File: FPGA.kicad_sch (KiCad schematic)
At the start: 19 parts, among them U3 XC7A100T-FTG256, U5 S25FL127S

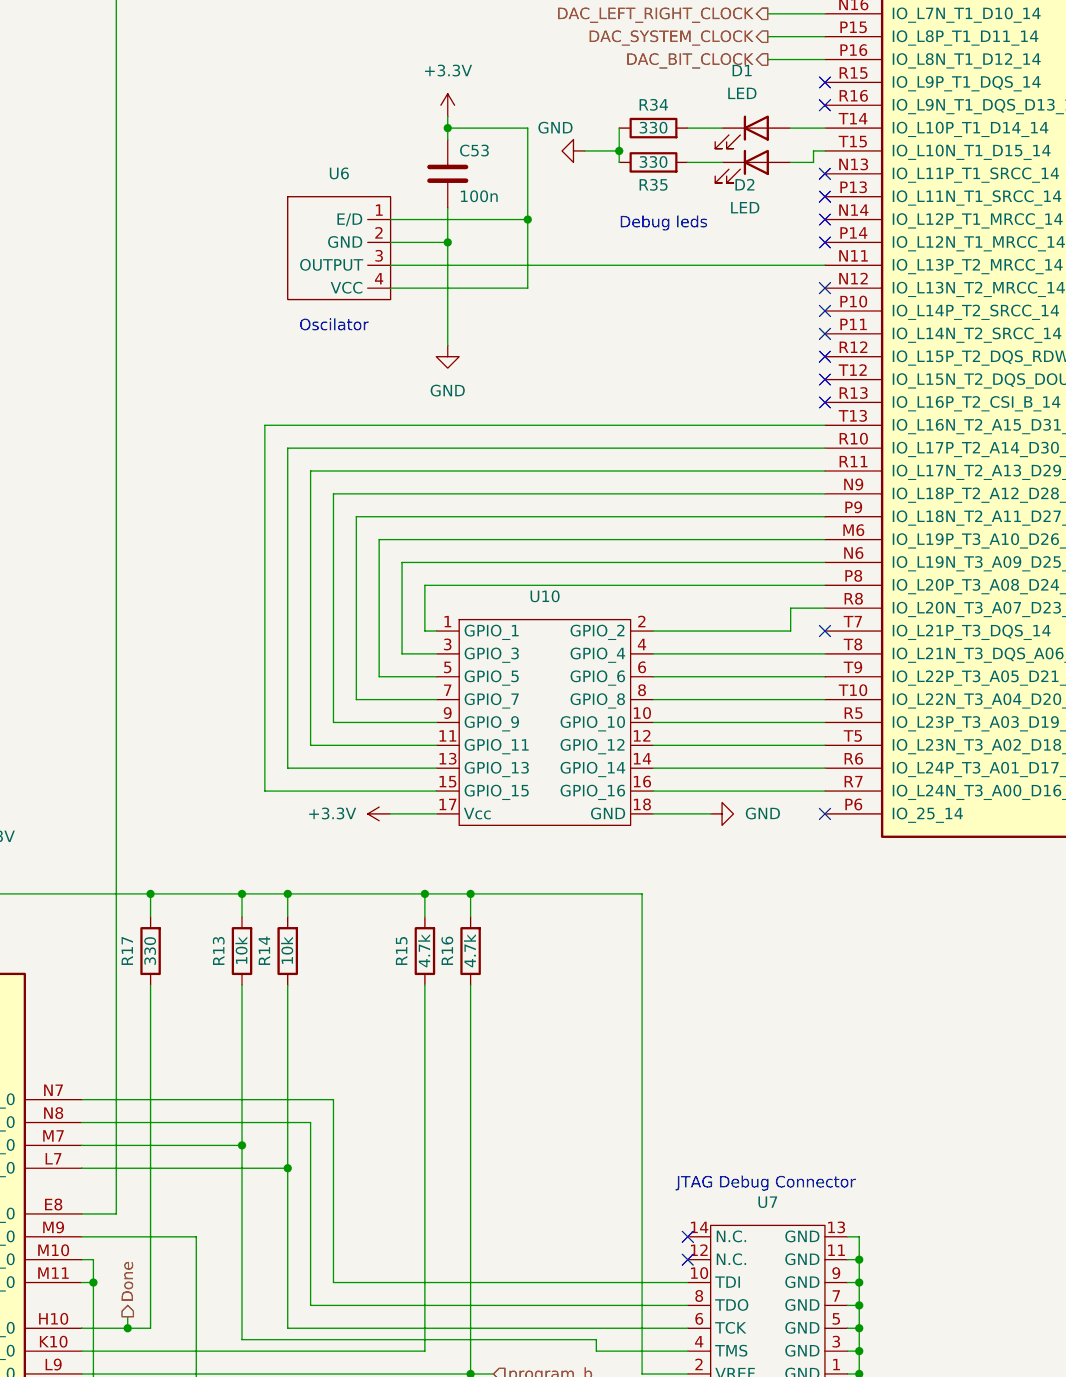
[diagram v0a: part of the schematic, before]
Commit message: Added footprints to symbols
Some nice light work
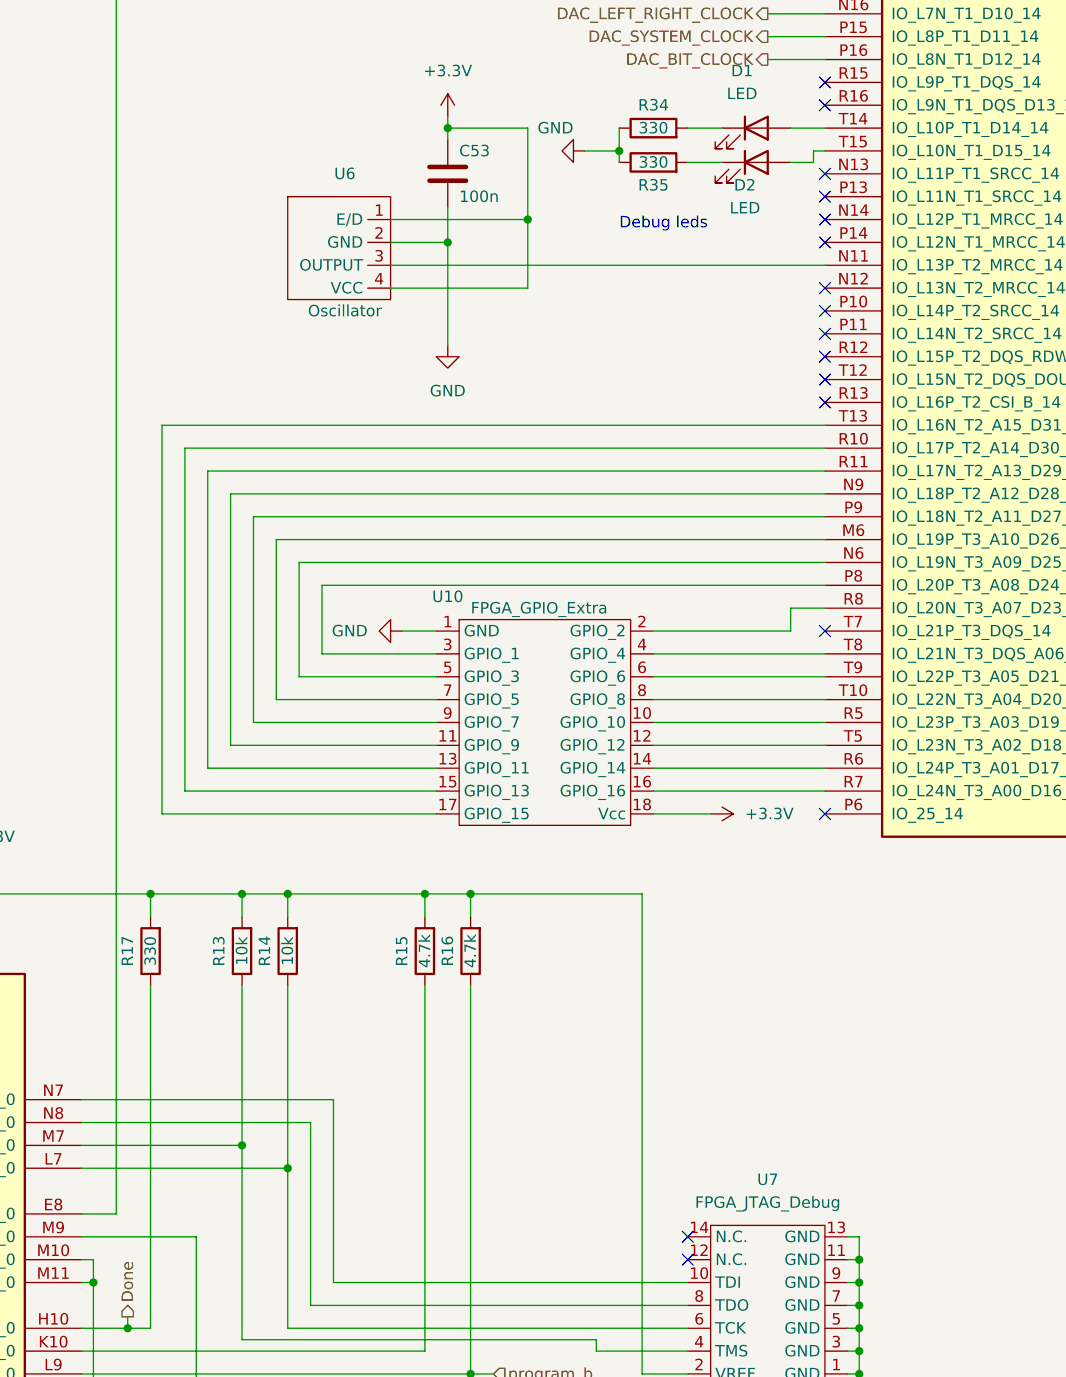
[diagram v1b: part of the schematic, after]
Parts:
- C52, C53: footprint (none) -> Capacitor_SMD:C_1206_3216Metric
- D1, D2: footprint (none) -> LED_SMD:LED_1812_4532Metric
- R10, R11, R12, R13, R14, R15, R16, R17, R34, R35: footprint (none) -> Resistor_SMD:R_1206_3216Metric
- U10: value ~ -> FPGA_GPIO_Extra; footprint (none) -> Connector_PinHeader_2.54mm:PinHeader_2x09_P2.54mm_Vertical
- U3: footprint (none) -> Package_BGA:Xilinx_FTG256
- U5: footprint (none) -> Package_SO:SOIC-8-1EP_3.9x4.9mm_P1.27mm_EP2.41x3.81mm
- U6: value ~ -> Oscillator; footprint (none) -> Oscillator:Oscillator_SMD_Abracon_ASE-4Pin_3.2x2.5mm_HandSoldering
- U7: value ~ -> FPGA_JTAG_Debug; footprint (none) -> Connector_PinHeader_2.54mm:PinHeader_2x07_P2.54mm_Vertical
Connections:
- net +3.3V: now also U10.18 (Vcc); no longer U10.17 (Vcc)
- net GND: now also U10.1 (GND); no longer U10.18 (GND)
- net at U3.M6 (IO_L19P_T3_A10_D26_14): now also U10.7 (GPIO_5); no longer U10.5 (GPIO_5)
- net at U3.N6 (IO_L19N_T3_A09_D25_VREF_14): now also U10.5 (GPIO_3); no longer U10.3 (GPIO_3)
- net at U3.N9 (IO_L18P_T2_A12_D28_14): now also U10.11 (GPIO_9); no longer U10.9 (GPIO_9)
- net at U3.P8 (IO_L20P_T3_A08_D24_14): now also U10.3 (GPIO_1); no longer U10.1 (GPIO_1)
- net at U3.P9 (IO_L18N_T2_A11_D27_14): now also U10.9 (GPIO_7); no longer U10.7 (GPIO_7)
- net at U3.R10 (IO_L17P_T2_A14_D30_14): now also U10.15 (GPIO_13); no longer U10.13 (GPIO_13)
- net at U3.R11 (IO_L17N_T2_A13_D29_14): now also U10.13 (GPIO_11); no longer U10.11 (GPIO_11)
- net at U3.T13 (IO_L16N_T2_A15_D31_14): now also U10.17 (GPIO_15); no longer U10.15 (GPIO_15)
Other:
- note removed: "JTAG Debug Connector"
- note removed: "Oscilator"

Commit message: Started implementing physical layout
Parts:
- U5: footprint Package_SO:SOIC-8-1EP_3.9x4.9mm_P1.27mm_EP2.41x3.81mm -> Package_SO:SOIC-8W_5.3x5.3mm_P1.27mm
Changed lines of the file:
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@@
       (effects (font (size 1.27 1.27)))
     )
-    (property "Footprint" "Package_SO:SOIC-8-1EP_3.9x4.9mm_P1.27mm_EP2.41x3.81mm" (at 77.47 72.39 0)
+    (property "Footprint" "Package_SO:SOIC-8W_5.3x5.3mm_P1.27mm" (at 77.47 72.39 0)
       (effects (font (size 1.27 1.27)) hide)
     )

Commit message: Changed Reistor and Capacitor size fomr 1206 to 0805
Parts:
- C52, C53: footprint Capacitor_SMD:C_1206_3216Metric -> Capacitor_SMD:C_0805_2012Metric
- R10, R11, R12, R13, R14, R15, R16, R17, R34, R35: footprint Resistor_SMD:R_1206_3216Metric -> Resistor_SMD:R_0805_2012Metric
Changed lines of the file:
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@@
       (effects (font (size 1.27 1.27)) (justify left))
     )
-    (property "Footprint" "Capacitor_SMD:C_1206_3216Metric" (at 143.2052 106.68 0)
+    (property "Footprint" "Capacitor_SMD:C_0805_2012Metric" (at 143.2052 106.68 0)
       (effects (font (size 1.27 1.27)) hide)
     )
@@
       (effects (font (size 1.27 1.27)))
     )
-    (property "Footprint" "Resistor_SMD:R_1206_3216Metric" (at 141.478 189.23 90)
+    (property "Footprint" "Resistor_SMD:R_0805_2012Metric" (at 141.478 189.23 90)
       (effects (font (size 1.27 1.27)) hide)
     )
@@
       (effects (font (size 1.27 1.27)))
     )
-    (property "Footprint" "Resistor_SMD:R_1206_3216Metric" (at 126.238 189.23 90)
+    (property "Footprint" "Resistor_SMD:R_0805_2012Metric" (at 126.238 189.23 90)
       (effects (font (size 1.27 1.27)) hide)
     )
@@
       (effects (font (size 1.27 1.27)))
     )
-    (property "Footprint" "Resistor_SMD:R_1206_3216Metric" (at 146.558 189.23 90)
+    (property "Footprint" "Resistor_SMD:R_0805_2012Metric" (at 146.558 189.23 90)
       (effects (font (size 1.27 1.27)) hide)
     )
@@
       (effects (font (size 1.27 1.27)))
     )
-    (property "Footprint" "Resistor_SMD:R_1206_3216Metric" (at 110.998 189.23 90)
+    (property "Footprint" "Resistor_SMD:R_0805_2012Metric" (at 110.998 189.23 90)
       (effects (font (size 1.27 1.27)) hide)
     )
@@
       (effects (font (size 1.27 1.27)))
     )
-    (property "Footprint" "Resistor_SMD:R_1206_3216Metric" (at 81.788 49.53 90)
+    (property "Footprint" "Resistor_SMD:R_0805_2012Metric" (at 81.788 49.53 90)
       (effects (font (size 1.27 1.27)) hide)
     )
@@
       (effects (font (size 1.27 1.27)))
     )
-    (property "Footprint" "Resistor_SMD:R_1206_3216Metric" (at 121.158 189.23 90)
+    (property "Footprint" "Resistor_SMD:R_0805_2012Metric" (at 121.158 189.23 90)
       (effects (font (size 1.27 1.27)) hide)
     )
@@
       (effects (font (size 1.27 1.27)) (justify left))
     )
-    (property "Footprint" "Capacitor_SMD:C_1206_3216Metric" (at 49.2252 62.23 0)
+    (property "Footprint" "Capacitor_SMD:C_0805_2012Metric" (at 49.2252 62.23 0)
       (effects (font (size 1.27 1.27)) hide)
     )
@@
       (effects (font (size 1.27 1.27)))
     )
-    (property "Footprint" "Resistor_SMD:R_1206_3216Metric" (at 165.1 103.378 90)
+    (property "Footprint" "Resistor_SMD:R_0805_2012Metric" (at 165.1 103.378 90)
       (effects (font (size 1.27 1.27)) hide)
     )
@@
       (effects (font (size 1.27 1.27)))
     )
-    (property "Footprint" "Resistor_SMD:R_1206_3216Metric" (at 165.1 99.568 90)
+    (property "Footprint" "Resistor_SMD:R_0805_2012Metric" (at 165.1 99.568 90)
       (effects (font (size 1.27 1.27)) hide)
     )
@@
       (effects (font (size 1.27 1.27)))
     )
-    (property "Footprint" "Resistor_SMD:R_1206_3216Metric" (at 112.268 49.53 90)
+    (property "Footprint" "Resistor_SMD:R_0805_2012Metric" (at 112.268 49.53 90)
       (effects (font (size 1.27 1.27)) hide)
     )
@@
       (effects (font (size 1.27 1.27)))
     )
-    (property "Footprint" "Resistor_SMD:R_1206_3216Metric" (at 62.738 50.8 90)
-      (effects (font (size 1.27 1.27)) hide)
-    )
+    (property "Footprint" "Resistor_SMD:R_0805_2012Metric" (at 62.738 50.8 90)
+      (effects (font (size 1.27 1.27)) hide)
+    )

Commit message: Changed MCU_Debug to 1.27mm pitch
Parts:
- U7: footprint Connector_PinHeader_2.54mm:PinHeader_2x07_P2.54mm_Vertical -> Connector_PinSocket_2.00mm:PinSocket_2x07_P2.00mm_Vertical
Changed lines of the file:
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@@
       (effects (font (size 1.27 1.27)))
     )
-    (property "Footprint" "Connector_PinHeader_2.54mm:PinHeader_2x07_P2.54mm_Vertical" (at 180.34 232.41 0)
+    (property "Footprint" "Connector_PinSocket_2.00mm:PinSocket_2x07_P2.00mm_Vertical" (at 180.34 232.41 0)
       (effects (font (size 1.27 1.27)) hide)
     )
